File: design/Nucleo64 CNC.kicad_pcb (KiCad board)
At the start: 4 copper layers, 76 x 82.5 mm, 99 parts, among them J1 YMotor, J10 ZB, J11 AA, J12 AB, J13 VMOT, J14 Spindle/Coolant, J15 Control, J16 I2C, J17 UART/GPIO, J18 Limits, J19 GPIO, J2 XMotor, J20 Power out, J21 SDCARD/GPIO, J23 Reset, J24 DC Spindle, J3 ZMotor, J4 AMotor, J5 YA, J6 YB, J7 XA, J8 XB, J9 ZA, Q1 2N7002, Q2 IRLML6402, Q3 2N7002, U1 NUCLEO64-F411RE, U10 74LVC2G17, U2 TLP290-4, U3 TLP290-4, U4 TLP290-4, U5 24LC16, U6 TCA9406, U7 ULN2003, U8 TLP290-4, U9 74LVC1G17

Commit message: Updated
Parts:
- added C8: 2u2, Capacitor_SMD:C_1206_3216Metric, B.Cu at (39.2, -30.0)
- added C9: 1u, Capacitor_SMD:C_1206_3216Metric, B.Cu at (32.6, -30.0)
- added R37: 1M, Resistor_SMD:R_0805_2012Metric, B.Cu at (62.3, -15.6)
- added REF**: OSHW-Logo2_9.8x8mm_SilkScreen, Symbol:OSHW-Logo2_9.8x8mm_SilkScreen, F.Cu at (28.5, -45.3)
- added U11: 74LVC1G17, Package_TO_SOT_SMD:SOT-353_SC-70-5, B.Cu at (59.7, -11.0)
- added U12: TPS709, Package_TO_SOT_SMD:SOT-23-5, B.Cu at (35.9, -31.4)
- C5: value C -> 100n
- Lk6: value DC Spindle -> LDObypass
- moved Lk6 27.5 mm to (35.5, -28.1)
- moved R36 20.0 mm to (63.7, -30.0)
- moved C6 20.0 mm to (20.3, -40.7)
- moved R25 20.0 mm to (25.7, -47.9)
- moved C5 20.0 mm to (21.5, -45.7)
- moved R34 20.0 mm to (23.6, -45.7)
- moved J21 20.0 mm to (48.0, -49.5)
- moved Lk4 20.0 mm to (11.6, -42.3)
- moved Q1 20.0 mm to (47.5, -37.8)
- moved Q3 20.0 mm to (53.5, -37.8)
- moved R18 20.0 mm to (15.2, -39.2)
- moved R30 20.0 mm to (50.5, -41.9)
- moved R32 20.0 mm to (56.7, -38.7)
- moved U1 20.0 mm to (6.30, -49.5)
- moved A1 20.0 mm to (35.9, -54.6)
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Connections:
- J14 pad 1: Net-(J14-Pad1) -> GNDS
- J14 pad 11: Net-(J14-Pad1) -> GNDS
- J14 pad 13: Net-(J14-Pad1) -> GNDS
- J14 pad 16: /SpindlePWM -> /SpindlePWMOut
- J14 pad 3: Net-(J14-Pad1) -> GNDS
- J14 pad 5: Net-(J14-Pad1) -> GNDS
- J14 pad 7: Net-(J14-Pad1) -> GNDS
- J14 pad 9: Net-(J14-Pad1) -> GNDS
- J15 pad 1: GND -> GNDS
- J15 pad 3: GND -> GNDS
- J15 pad 5: GND -> GNDS
- J15 pad 7: GND -> GNDS
- J15 pad 9: GND -> GNDS
- J18 pad 1: GND -> GNDS
- J18 pad 3: GND -> GNDS
- J18 pad 5: GND -> GNDS
- J18 pad 7: GND -> GNDS
- Lk1 pad 2: Net-(Lk1-Pad2) -> Vdrive
- Lk3 pad 2: Net-(J14-Pad1) -> GNDS
- Lk6 pad 1: /SpindlePWM -> Vdrive
- Lk6 pad 2: Net-(Lk6-Pad2) -> Net-(C8-Pad1)
- R1 pad 1: +5V -> Vdrive
- R2 pad 1: +5V -> Vdrive
- R24 pad 1: +5V -> Vdrive
- R4 pad 1: +5V -> Vdrive
- R5 pad 1: +5V -> Vdrive
- R6 pad 1: +5V -> Vdrive
- R7 pad 1: +5V -> Vdrive
- R8 pad 1: +5V -> Vdrive
- R9 pad 1: +5V -> Vdrive
- U1 pad 17: /STDiag1 -> /AuxIn1
- U1 pad 60: /AuxIn1 -> /AuxOut1
- U1 pad 63: /AuxOut1 -> /Flood
- U1 pad 64: /AuxIn0 -> /AuxOut0
- U1 pad 65: /Flood -> /Mist
- U1 pad 66: /AuxOut0 -> /AuxIn0
- U1 pad 68: /Mist -> /STDiag1
- U2 pad 11: GND -> GNDS
- U2 pad 13: GND -> GNDS
- U2 pad 15: GND -> GNDS
- U2 pad 9: GND -> GNDS
- U3 pad 11: GND -> GNDS
- U3 pad 13: GND -> GNDS
- U3 pad 15: GND -> GNDS
- U3 pad 9: GND -> GNDS
- U4 pad 10: Net-(Lk1-Pad2) -> Net-(C8-Pad1)
- U4 pad 12: Net-(Lk1-Pad2) -> Net-(C8-Pad1)
- U4 pad 14: Net-(Lk1-Pad2) -> Net-(C8-Pad1)
- U4 pad 16: Net-(Lk1-Pad2) -> Net-(C8-Pad1)
- U7 pad 7: Net-(J14-Pad1) -> GNDS
- U7 pad 8: Net-(J14-Pad1) -> GNDS
- U7 pad 9: Net-(Lk1-Pad2) -> Net-(U7-Pad9)
- U8 pad 14: Net-(Lk1-Pad2) -> Net-(C8-Pad1)
- U8 pad 16: Net-(Lk1-Pad2) -> Net-(C8-Pad1)
- U8 pad 6: Net-(Lk6-Pad2) -> /SpindlePWMOut
- U8 pad 9: GND -> GNDS
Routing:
- net GNDS: track 0.00 -> 153.8 mm, vias 0 -> 9
- net Vdrive: track 0.00 -> 112.7 mm, vias 0 -> 8
- net /AuxIn1: track 15.9 -> 71.3 mm, vias 1 -> 2
- net Net-(Lk1-Pad2): track 47.5 -> 0.00 mm
- net Net-(C8-Pad1): track 0.00 -> 36.8 mm
- net /SpindlePWMOut: track 0.00 -> 35.5 mm, vias 0 -> 1
- net Net-(J14-Pad1): track 33.3 -> 0.00 mm
- net +5V: track 112.2 -> 79.4 mm, vias 8 -> 0
- net /SpindlePWM: track 37.5 -> 14.8 mm
- net Net-(J15-Pad2): track 64.3 -> 82.7 mm
- net /STDiag1: track 107.9 -> 125.8 mm
- net GND: track 98.6 -> 115.7 mm, vias 14 -> 7
- net Net-(Lk6-Pad2): track 14.8 -> 0.00 mm
- net /Mist: track 30.8 -> 25.8 mm
- net /ALim: track 42.0 -> 44.9 mm
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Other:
- board text added: "Rev. 1.0"
- board text added: "©2020 Terje Io"

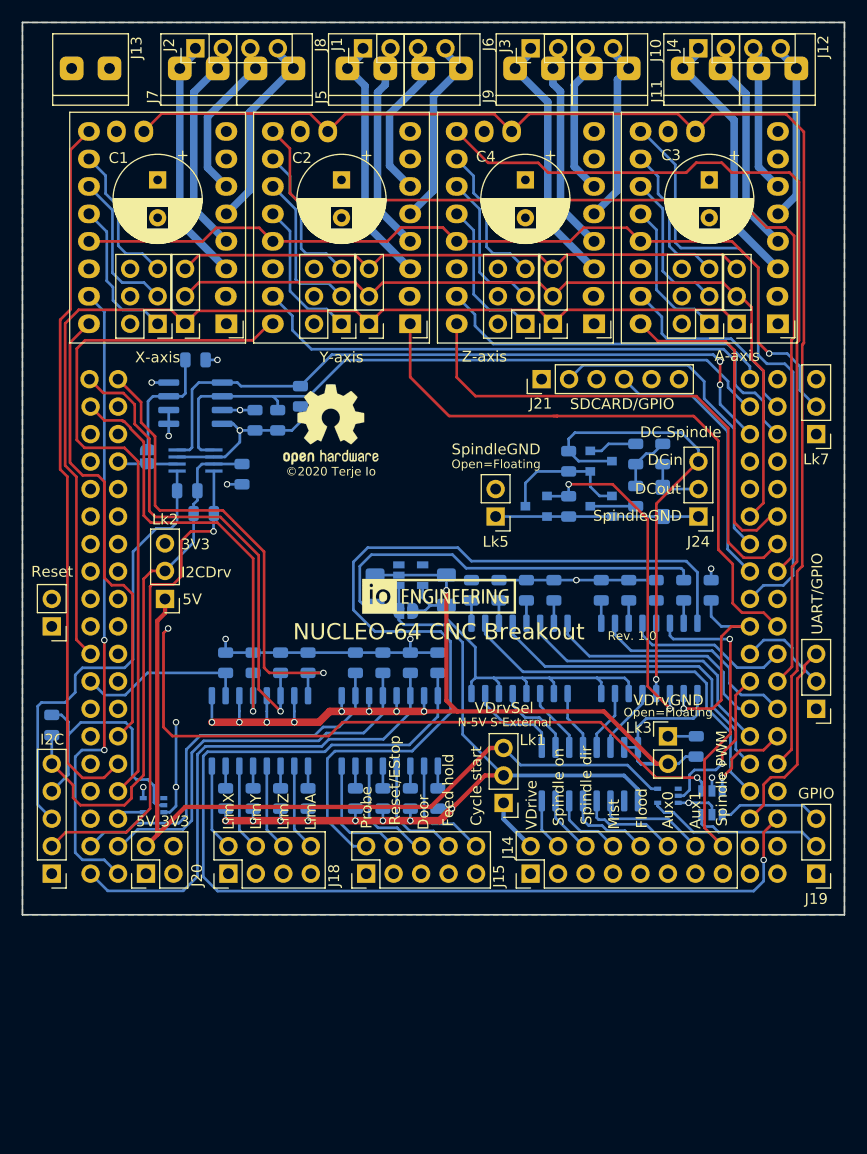
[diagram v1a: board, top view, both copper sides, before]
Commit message: Updated to version sent for small prototype batch
Design and board map file to be verified with this batch.
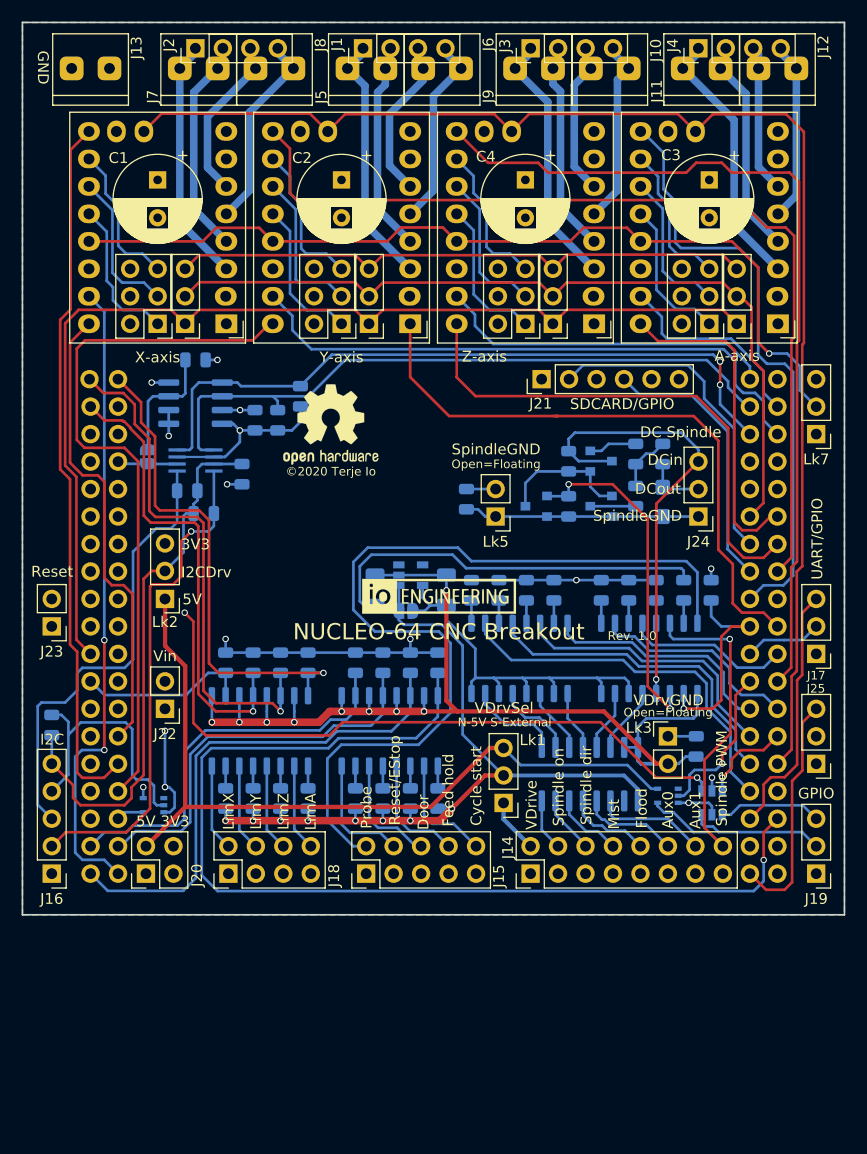
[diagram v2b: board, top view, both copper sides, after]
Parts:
- added J22: Vin, Connector_PinHeader_2.54mm:PinHeader_1x02_P2.54mm_Vertical, F.Cu at (13.2, -19.0)
- added J25: UART1, Connector_PinHeader_2.54mm:PinHeader_1x03_P2.54mm_Vertical, F.Cu at (73.4, -14.0)
- added R38: 1M, Resistor_SMD:R_0805_2012Metric, B.Cu at (41.0, -38.4)
- U12: value TPS709 -> TPS70939
- moved J17 5.08 mm to (73.4, -24.1)
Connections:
- U1 pad 4: Net-(U1-Pad4) -> /AuxIn1
- U7 pad 9: Net-(U7-Pad9) -> Vdrive
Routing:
- net Net-(J25-Pad3): track 0.00 -> 21.8 mm
- net /AuxIn1: track 71.3 -> 89.7 mm
- net Net-(J25-Pad2): track 0.00 -> 13.8 mm
- net /UARTRX: track 18.5 -> 23.6 mm
- net Net-(J22-Pad2): track 0.00 -> 4.34 mm
- net Net-(C7-Pad2): track 18.8 -> 21.7 mm
- net GND: track 115.7 -> 118.1 mm
- net +5V: track 79.4 -> 77.2 mm
- net /ZLim: track 46.2 -> 48.0 mm
- net /UARTTX: track 8.75 -> 7.18 mm
- net GNDS: track 153.8 -> 152.3 mm
- net /ALim: track 44.9 -> 46.4 mm
- net /YLim: track 42.7 -> 43.5 mm
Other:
- rule pad_to_mask_clearance: 0.2 -> 0
- board text added: "+"
- board text added: "GND"

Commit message: Updated to v1.0c
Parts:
- added Lk10: AA, Connector_PinHeader_2.54mm:PinHeader_1x02_P2.54mm_Vertical, F.Cu at (25.7, -57.2)
- added Lk11: AA, Connector_PinHeader_2.54mm:PinHeader_1x02_P2.54mm_Vertical, F.Cu at (42.7, -57.2)
- added Lk12: AA, Connector_PinHeader_2.54mm:PinHeader_1x02_P2.54mm_Vertical, F.Cu at (59.7, -57.2)
- added Lk13: TMC UART, Connector_PinHeader_2.54mm:PinHeader_1x02_P2.54mm_Vertical, F.Cu at (73.4, -36.8)
- added Lk8: TMC UART/SPI, Connector_PinHeader_2.54mm:PinHeader_1x03_P2.54mm_Vertical, F.Cu at (73.4, -44.4)
- added Lk9: AA, Connector_PinHeader_2.54mm:PinHeader_1x02_P2.54mm_Vertical, F.Cu at (8.69, -57.2)
- added R39: 1K, Resistor_SMD:R_0805_2012Metric, B.Cu at (73.1, -41.9)
- added R40: 470, Resistor_SMD:R_0805_2012Metric, B.Cu at (61.1, -30.0)
- added R41: 2K2, Resistor_SMD:R_0805_2012Metric, B.Cu at (63.7, -16.6)
- added R42: 10K, Resistor_SMD:R_0805_2012Metric, B.Cu at (73.4, -14.0)
- added R43: 10K, Resistor_SMD:R_0805_2012Metric, B.Cu at (60.2, -9.50)
- added U13: VOM452, Package_SO:MFSOP6-5_4.4x3.6mm_P1.27mm, B.Cu at (37.2, -37.5)
- C7: value 4u7 -> 10u
- J17: value UART/GPIO -> UART
- J19: footprint Connector_PinHeader_2.54mm:PinHeader_1x03_P2.54mm_Vertical -> Connector_PinHeader_2.54mm:PinHeader_1x04_P2.54mm_Vertical
- Lk7: value TRINAMIC SPI -> TMC DATA
- R28: value 150 -> 1K8
- R30: value 470 -> 1K
- moved R28 27.5 mm to (32.0, -37.2)
- moved Lk7 10.2 mm to (73.4, -54.6)
- moved R29 4.66 mm to (48.4, -41.9)
- moved LkAb1 3.81 mm to (62.2, -54.6)
- moved LkAa1 3.81 mm to (67.3, -54.6)
- moved LkYa1 3.81 mm to (33.3, -54.6)
- moved LkZa1 3.81 mm to (50.3, -54.6)
- moved LkZb1 3.81 mm to (45.2, -54.6)
- moved LkXa1 3.81 mm to (16.3, -54.6)
- moved LkXb1 3.81 mm to (11.2, -54.6)
- moved LkYb2 3.81 mm to (28.2, -54.6)
- moved J17 2.54 mm to (73.4, -26.7)
- moved J25 2.54 mm to (73.4, -16.5)
- moved R24 2.54 mm to (58.6, -30.0)
- moved Q1 2.30 mm to (49.8, -37.8)
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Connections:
- A1 pad 13: /SDOd -> /SDIz
- A1 pad 14: Net-(A1-Pad14) -> /SDOd
- A1 pad 17: /STDiag1 -> /YLim
- A2 pad 13: /SDOd -> /SDIy
- A2 pad 14: Net-(A2-Pad14) -> /SDOd
- A2 pad 17: /STDiag1 -> /XLim
- A3 pad 13: /SDOd -> /SDIa
- A3 pad 14: Net-(A3-Pad14) -> /SDOd
- A3 pad 17: /STDiag1 -> /ZLim
- A4 pad 13: /SDOd -> /SDOt
- A4 pad 14: Net-(A4-Pad14) -> /SDOd
- A4 pad 17: /STDiag1 -> /ALim
- Lk7 pad 1: /SDO -> Net-(Lk7-Pad1)
- Lk7 pad 2: /SDOd -> /SDOt
- LkAa1 pad 1: Net-(A4-Pad12) -> +3V3
- LkAa1 pad 2: +3V3 -> Net-(A4-Pad12)
- LkAa1 pad 3: Net-(A4-Pad11) -> +3V3
- LkAa1 pad 4: +3V3 -> Net-(A4-Pad11)
- LkAa1 pad 5: Net-(A4-Pad10) -> +3V3
- LkAa1 pad 6: +3V3 -> Net-(A4-Pad10)
- LkAb1 pad 3: /SDI -> /SDIa
- LkXa1 pad 1: Net-(A2-Pad12) -> +3V3
- LkXa1 pad 2: +3V3 -> Net-(A2-Pad12)
- LkXa1 pad 3: Net-(A2-Pad11) -> +3V3
- LkXa1 pad 4: +3V3 -> Net-(A2-Pad11)
- LkXa1 pad 5: Net-(A2-Pad10) -> +3V3
- LkXa1 pad 6: +3V3 -> Net-(A2-Pad10)
- LkYa1 pad 1: Net-(A1-Pad12) -> +3V3
- LkYa1 pad 2: +3V3 -> Net-(A1-Pad12)
- LkYa1 pad 3: Net-(A1-Pad11) -> +3V3
- LkYa1 pad 4: +3V3 -> Net-(A1-Pad11)
- LkYa1 pad 5: Net-(A1-Pad10) -> +3V3
- LkYa1 pad 6: +3V3 -> Net-(A1-Pad10)
- LkYb2 pad 3: /SDI -> /SDIy
- LkZa1 pad 1: Net-(A3-Pad12) -> +3V3
- LkZa1 pad 2: +3V3 -> Net-(A3-Pad12)
- LkZa1 pad 3: Net-(A3-Pad11) -> +3V3
- LkZa1 pad 4: +3V3 -> Net-(A3-Pad11)
- LkZa1 pad 5: Net-(A3-Pad10) -> +3V3
- LkZa1 pad 6: +3V3 -> Net-(A3-Pad10)
- LkZb1 pad 3: /SDI -> /SDIz
- Q2 pad 2: Net-(Q2-Pad2) -> Net-(J24-Pad3)
- Q2 pad 3: Net-(J24-Pad3) -> Net-(Q2-Pad3)
- R28 pad 1: +3V3 -> +5V
- R29 pad 1: Net-(Q1-Pad1) -> Net-(J24-Pad3)
- R29 pad 2: Net-(C7-Pad2) -> Net-(Q1-Pad1)
- R31 pad 1: Net-(Q2-Pad2) -> Net-(Q2-Pad3)
- U1 pad 68: /STDiag1 -> /AuxIn2
- U8 pad 10: /Probe -> /AuxIn2
- U8 pad 11: Net-(Q1-Pad1) -> GNDS
- U8 pad 12: Net-(J24-Pad3) -> /Probe
- U8 pad 5: Net-(R28-Pad2) -> Net-(R24-Pad2)
- U8 pad 6: /SpindlePWMOut -> Net-(J15-Pad2)
- U8 pad 7: Net-(R24-Pad2) -> Net-(R40-Pad2)
- U8 pad 8: Net-(J15-Pad2) -> Net-(J19-Pad4)
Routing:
- net /STDiag1: track 125.8 -> 0.00 mm
- net /ALim: track 46.4 -> 133.1 mm, vias 1 -> 2
- net /XLim: track 16.0 -> 84.7 mm, vias 0 -> 1
- net /ZLim: track 48.0 -> 115.6 mm, vias 1 -> 2
- net VDDF: track 0.00 -> 52.7 mm
- net /YLim: track 43.5 -> 95.1 mm, vias 1 -> 2
- net GND: track 118.1 -> 157.8 mm, vias 7 -> 8
- net /SpindlePWMOut: track 35.5 -> 64.2 mm
- net /SDIa: track 0.00 -> 26.8 mm
- net /SDIz: track 0.00 -> 26.7 mm
- net /SDIy: track 0.00 -> 26.7 mm
- net Net-(J19-Pad4): track 0.00 -> 24.5 mm
- net +5V: track 77.2 -> 100.8 mm
- net /SDOt: track 0.00 -> 22.6 mm, vias 0 -> 1
- net /SCK: track 85.8 -> 105.5 mm
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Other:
- board text added: "Rev. 1.0c"
- board text removed: "Rev. 1.0"
